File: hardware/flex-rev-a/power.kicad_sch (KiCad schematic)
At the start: 21 parts, among them SW201 button DNP, U201 nPM1304-QEAA

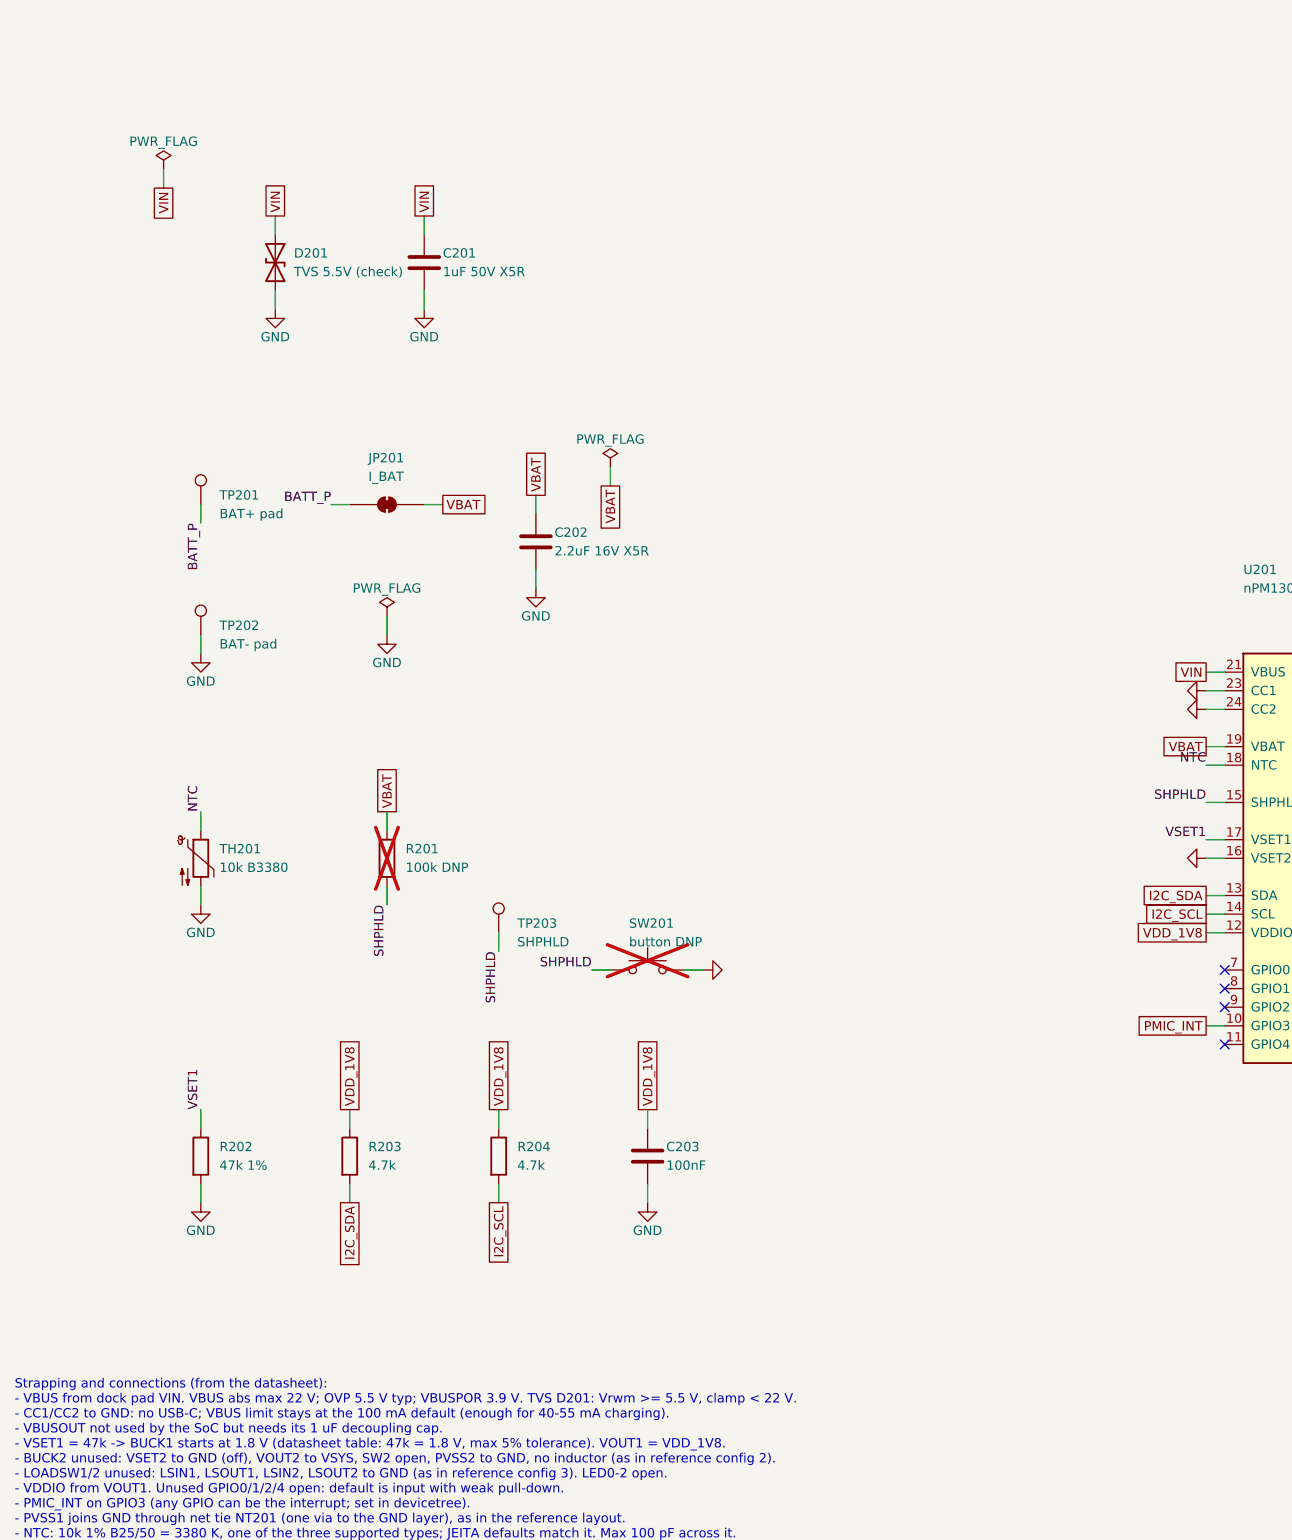
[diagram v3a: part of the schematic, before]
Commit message: Draw dock sheet: six pogo pads with TVS and series resistors
- J601: six pads at 2 mm pitch, 1.2 x 3.0 mm (project footprint), order
  VIN, GND, SWDCLK, SWDIO, UART_RX, UART_TX.
- TPD1E10B06 TVS at the VIN pad and each data pad (D601-D605); none on
  the GND pad.
- 100 ohm in series between each data pad and the SoC net; 100k
  pull-down on UART_RX at the SoC side.
- VIN TVS and its PWR_FLAG move from the power sheet to the pad (the pads
  and the PMIC sit on different flex islands).
- (check) TPD1E10B06 leakage is 100 nA max at 5 V, above the 50 nA target;
  no 1.8 V figure for the data pads.

ERC: 1 error (nRESET, debug sheet next), 3 warnings; SWDCLK error cleared.

Co-Authored-By: Claude Opus 5.5 <noreply@anthropic.com>
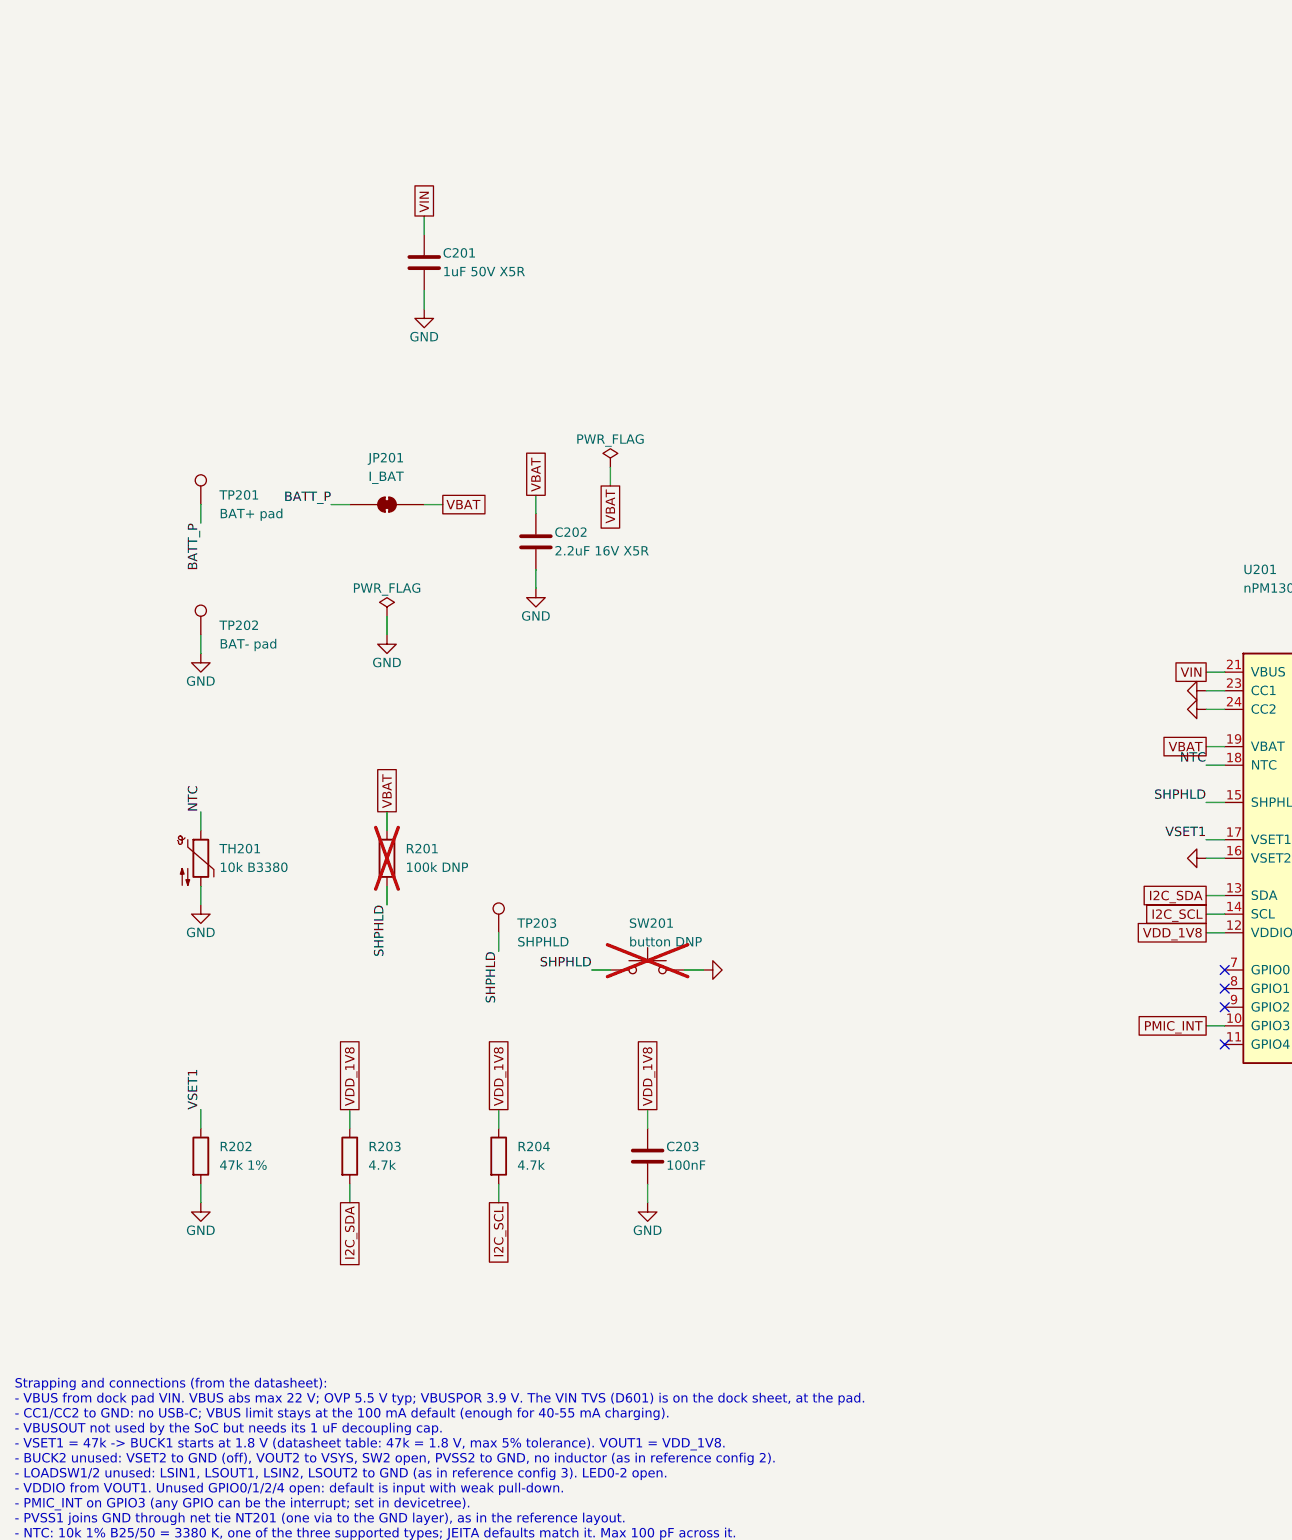
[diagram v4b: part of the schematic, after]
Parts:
- removed D201: TVS 5.5V (check), Diode_SMD:D_0402_1005Metric, symbol Device:D_TVS
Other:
- note added: "Strapping and connections (from the datasheet): - VBUS from dock pad VIN. VBUS abs max 22 V; OVP 5.5 V typ; VBUSPOR 3.9 V. The VIN TVS (D601) is on the dock sheet, at the pad. - CC1/CC2 to GND: no USB-C; VBUS limit stays at the 100 mA default (enough for 40-55 mA charging). - VBUSOUT not used by the SoC but needs its 1 uF decoupling cap. - VSET1 = 47k -> BUCK1 starts at 1.8 V (datasheet table: 47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"
- note removed: "Strapping and connections (from the datasheet): - VBUS from dock pad VIN. VBUS abs max 22 V; OVP 5.5 V typ; VBUSPOR 3.9 V. TVS D201: Vrwm >= 5.5 V, clamp < 22 V. - CC1/CC2 to GND: no USB-C; VBUS limit stays at the 100 mA default (enough for 40-55 mA charging). - VBUSOUT not used by the SoC but needs its 1 uF decoupling cap. - VSET1 = 47k -> BUCK1 starts at 1.8 V (datasheet table: 47k = 1.8 V, max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"

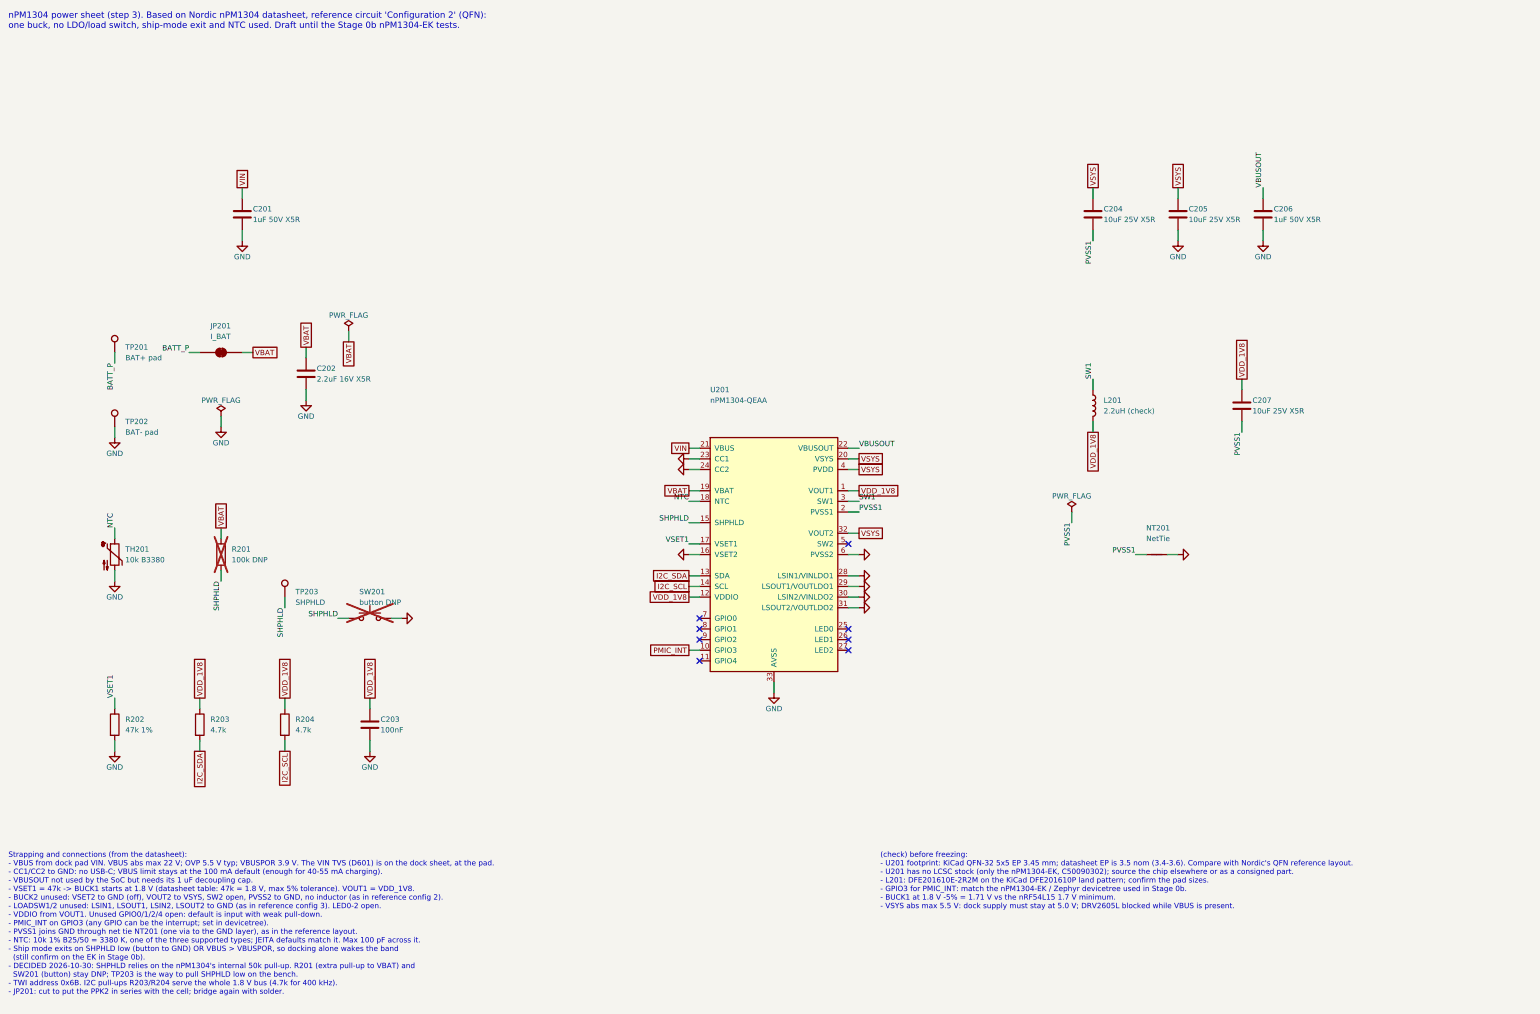
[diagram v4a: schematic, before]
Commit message: Apply schematic review fixes: 2.0 V rail, pad 10 NC, VIN TVS, bulk cap
- Power: R202 47k -> 68k so BUCK1 starts at 2.0 V; global net VDD_1V8
  renamed VDD_2V0 on every sheet, notes updated.
- Haptics: DRV2605L IN/TRIG tied to GND, HAPT_TRIG removed (effects run
  over I2C). Footprint kept as Package_SO:TSSOP-10_3x3mm_P0.5mm: it is
  KiCad's TI DGS land pattern (cites MPDS035); KiCad 10 has no footprint
  named VSSOP-10_3x3mm_P0.5mm.
- MCU: pad 10 (P1.10) no-connect; GND global label replaced by the GND
  power symbol; note on the trapped lower-row GND pads 12/14/16/18 and on
  pads 8/24.
- Sensors: C403 10 uF on LIS2DW12 VDD per ST; related (check) removed.
- Dock: VIN TVS is now Littelfuse SMF18A (SOD-123FL, 18 V standoff, LCSC
  C409420); data pads keep TPD1E10B06, TPD1E0B04 noted as a lower-leakage
  alternative (check).
- bom.csv regenerated, PDF replotted, README updated.

ERC: 0 errors, 0 warnings.

Co-Authored-By: Claude Opus 5.5 <noreply@anthropic.com>
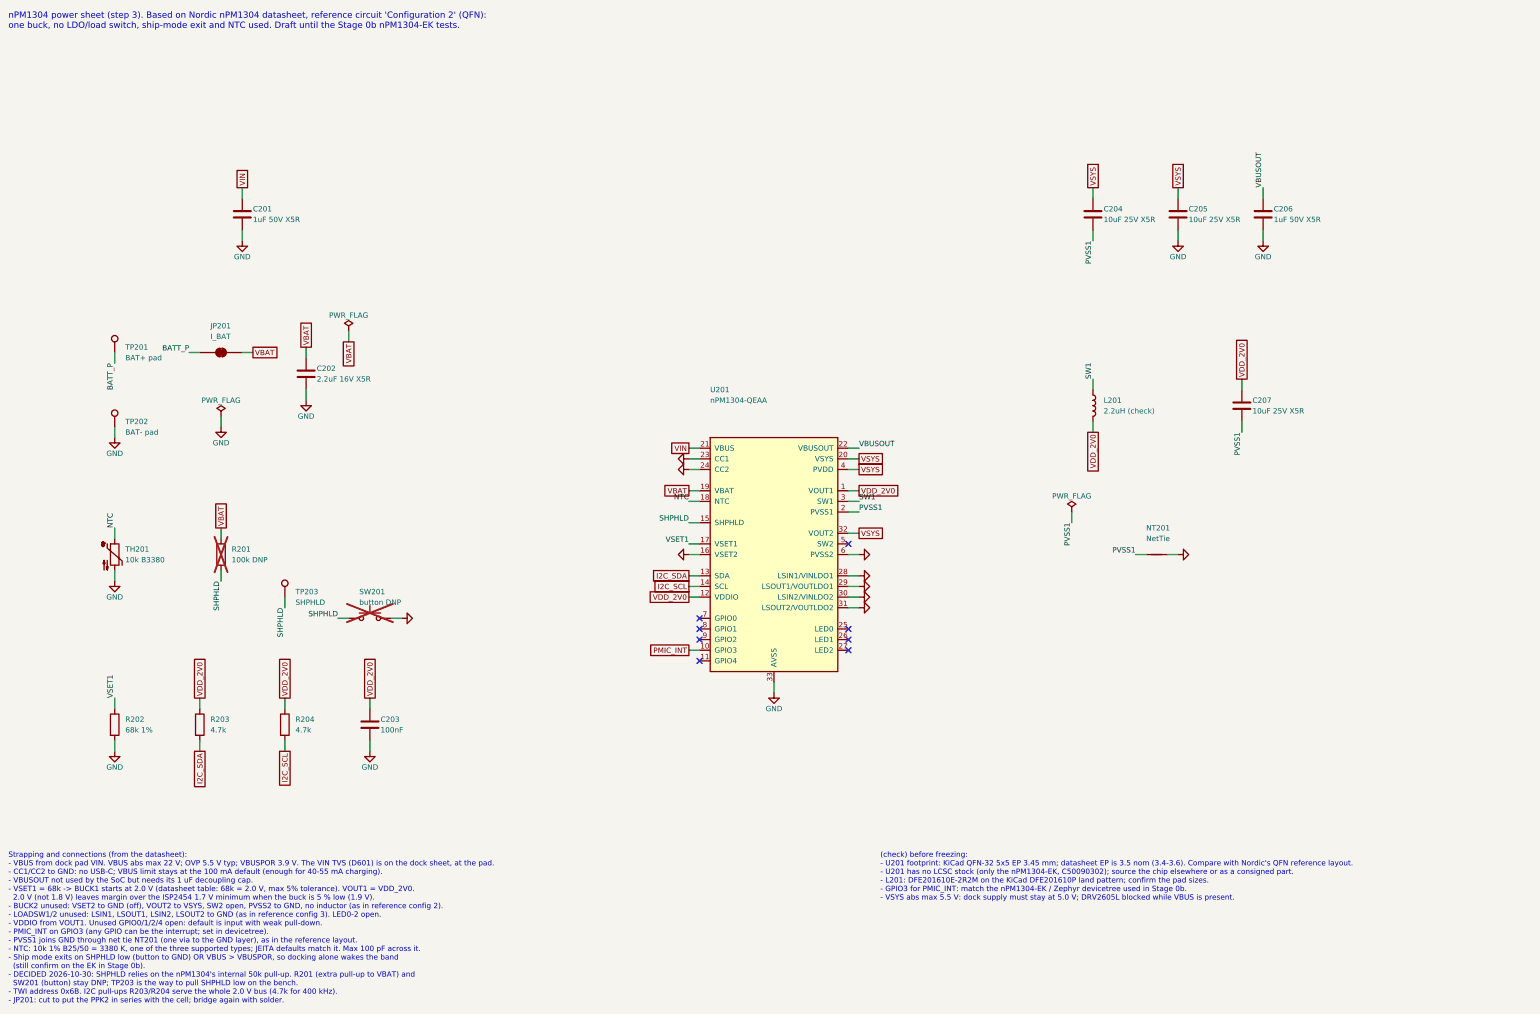
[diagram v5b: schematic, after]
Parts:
- R202: value 47k 1% -> 68k 1%; LCSC C25792 -> C36871
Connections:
- net VDD_1V8 renamed VDD_2V0
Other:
- note added: "Strapping and connections (from the datasheet): - VBUS from dock pad VIN. VBUS abs max 22 V; OVP 5.5 V typ; VBUSPOR 3.9 V. The VIN TVS (D601) is on the dock sheet, at the pad. - CC1/CC2 to GND: no USB-C; VBUS limit stays at the 100 mA default (enough for 40-55 mA charging). - VBUSOUT not used by the SoC but needs its 1 uF decoupling cap. - VSET1 = 68k -> BUCK1 starts at 2.0 V (datasheet table: 68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"
- note removed: "Strapping and connections (from the datasheet): - VBUS from dock pad VIN. VBUS abs max 22 V; OVP 5.5 V typ; VBUSPOR 3.9 V. The VIN TVS (D601) is on the dock sheet, at the pad. - CC1/CC2 to GND: no USB-C; VBUS limit stays at the 100 mA default (enough for 40-55 mA charging). - VBUSOUT not used by the SoC but needs its 1 uF decoupling cap. - VSET1 = 47k -> BUCK1 starts at 1.8 V (datasheet table: 47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"
